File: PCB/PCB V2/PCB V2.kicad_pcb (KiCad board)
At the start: 2 copper layers, 100 x 100 mm, 57 parts, among them J1 Screw_Terminal_01x03, J2 Screw_Terminal_01x03, J3 USB_B, J4 Conn_01x02_Pin, K1 Relay_SPDT, K2 Relay_SPDT, Q1 S8050, Q2 S8050, Q3 S8050, SW1 On/Off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

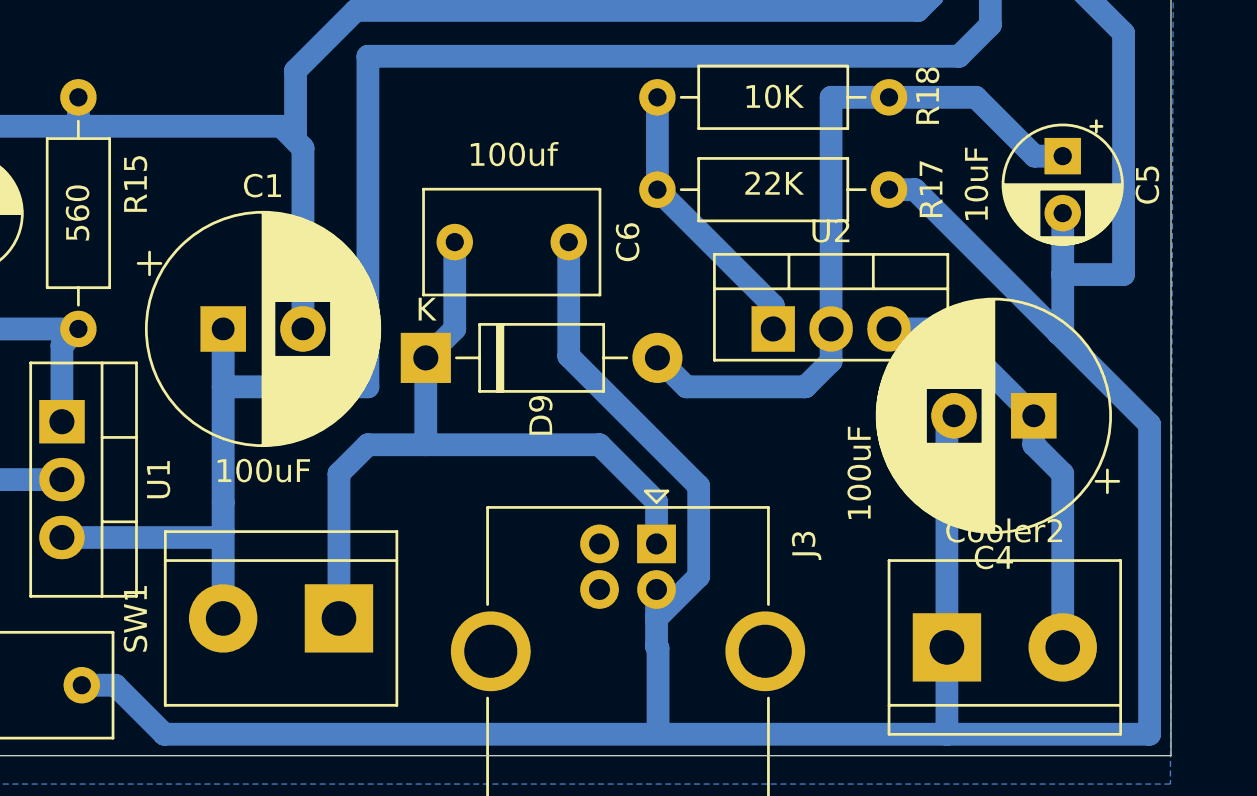
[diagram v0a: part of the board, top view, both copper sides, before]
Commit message: Cambiado el footprint del capacitor
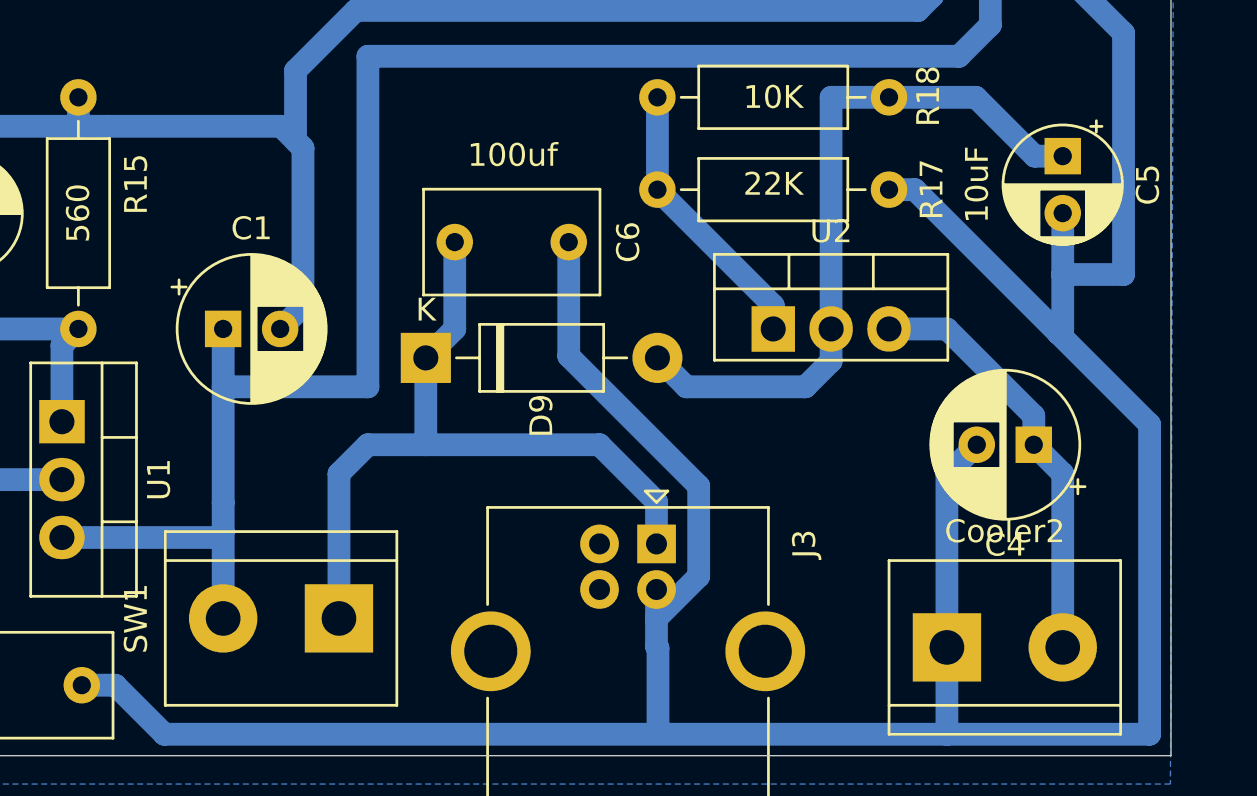
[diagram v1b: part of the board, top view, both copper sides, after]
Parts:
- C1, C4: footprint Capacitor_THT:CP_Radial_D10.0mm_P3.50mm -> Capacitor_THT:CP_Radial_D6.3mm_P2.50mm
- moved C4 1.27 mm to (194.3, 121.9)

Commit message: .
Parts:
- renumbered VCC2 to 3V3, VCC1 to 5V, Cooler2 to BATERIA
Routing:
- net +3.3V: track 339.2 -> 345.3 mm
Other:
- board text added: "GND"
- board text added: "SCL"
- board text added: "SDA"
- board text added: "VCC"
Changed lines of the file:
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@@
 		)
 		(fp_text user "INA219"
-			(at 10.16 0.23 -90)
-			(layer "F.Fab")
+			(at 10.16 0.23 270)
+			(layer "F.SilkS")
 			(effects
 				(font
@@
 		(at 201.295 69.9375 -90)
 		(property "Reference" "ESP-1"
-			(at 0 0.5 90)
+			(at 13.8825 22.225 90)
 			(layer "F.SilkS")
 			(effects
@@
 		(model "C:/Users/47698187/Documents/GitHub/Modelos-3D/Borneras - Conectores/Azules/Doble.step"
 			(offset
-				(xyz -10.25 -4.75 4)
+				(xyz -10.25 -4.75 5)
 			)
 			(scale
@@
 		)
 		(property "Value" "SW_Push"
-			(at -3.175 0 90)
+			(at -3.175 0 180)
 			(layer "F.SilkS")
 			(effects
@@
 		(descr "Through hole straight pin header, 1x01, 2.54mm pitch, single row")
 		(tags "Through hole pin header THT 1x01 2.54mm single row")
-		(property "Reference" "VCC1"
+		(property "Reference" "5V"
 			(at 2.2606 -0.2032 90)
 			(layer "F.SilkS")
@@
 		)
 		(property "Value" "22K"
-			(at 5.08 2.37 180)
-			(layer "F.Fab")
+			(at 5.08 0.179106 180)
+			(layer "F.SilkS")
 			(effects
 				(font
@@
 		(tags "terminal block bornier2")
 		(property "Reference" "SW1"
-			(at 8.89 0 -90)
+			(at 2.54 6.35 -90)
 			(layer "F.SilkS")
 			(effects
@@
 		(model "C:/Users/47698187/Documents/GitHub/Modelos-3D/Borneras - Conectores/Azules/Doble.step"
 			(offset
-				(xyz 15.25 4.75 4.5)
+				(xyz 15.25 4.75 5)
 			)
 			(scale
@@
 		(descr "Through hole straight pin header, 1x01, 2.54mm pitch, single row")
 		(tags "Through hole pin header THT 1x01 2.54mm single row")
-		(property "Reference" "VCC2"
-			(at 0 -2.33 0)
+		(property "Reference" "3V3"
+			(at 3.81 0 90)
 			(layer "F.SilkS")
 			(effects
@@
 		(descr "simple 2-pin terminal block, pitch 5.08mm, revamped version of bornier2")
 		(tags "terminal block bornier2")
-		(property "Reference" "Cooler2"
-			(at 2.54 -5.08 0)
+		(property "Reference" "BATERIA"
+			(at -2.54 -5.08 0)
 			(layer "F.SilkS")
 			(effects
@@
 	)
 	(gr_line
-		(start 165.1 62.23)
-		(end 157.226 62.23)
+		(start 165.1 66.04)
+		(end 157.226 66.04)
 		(stroke
 			(width 1)
@@
 		)
 	)
+	(gr_text "SDA"
+		(at 160.591666 62.248821 0)
+		(layer "F.SilkS")
+		(effects
+			(font
+				(size 1 1)
+				(thickness 0.1)
+			)
+			(justify left bottom)
+		)
+	)
 	(gr_text "GRUPO8 5B"
 		(at 100.33 49.53 0)
@@
 		)
 	)
+	(gr_text "VCC"
+		(at 163.38223 62.214423 0)
+		(layer "F.SilkS")
+		(effects
+			(font
+				(size 1 1)
+				(thickness 0.1)
+			)
+			(justify left bottom)
+		)
+	)
+	(gr_text "GND"
+		(at 166.37 62.23 0)
+		(layer "F.SilkS")
+		(effects
+			(font
+				(size 1 1)
+				(thickness 0.1)
+			)
+			(justify left bottom)
+		)
+	)
+	(gr_text "SCL"
+		(at 157.48 62.23 0)
+		(layer "F.SilkS")
+		(effects
+			(font
+				(size 1 1)
+				(thickness 0.1)
+			)
+			(justify left bottom)
+		)
+	)
 	(via
 		(at 105.3084 40.7416)
@@
 	)
 	(segment
-		(start 157.285 62.23)
-		(end 165.1 62.23)
+		(start 161.095 66.037207)
+		(end 165.102793 66.037207)
+		(width 1)
+		(layer "F.Cu")
+		(net 3)
+	)
+	(segment
+		(start 161.095 66.04)
+		(end 161.095 66.037207)
+		(width 1)
+		(layer "F.Cu")
+		(net 3)
+	)
+	(segment
+		(start 157.285 66.04)
+		(end 161.095 66.04)
 		(width 1)
 		(layer "F.Cu")
@@
 	)
 	(via
-		(at 165.1 62.23)
+		(at 165.102793 66.037207)
 		(size 1.6)
 		(drill 0.8)
@@
 	)
 	(via
-		(at 157.285 62.23)
+		(at 157.285 66.04)
 		(size 1.6)
 		(drill 0.8)
@@
 	)
 	(segment
+		(start 157.285 66.04)
+		(end 157.285 42.985)
+		(width 1)
+		(layer "B.Cu")
+		(net 3)
+	)
+	(segment
 		(start 182.86 53.34)
 		(end 182.86 65.757167)
@@
 	)
 	(segment
+		(start 132.480151 39.81)
+		(end 129.38 42.910151)
+		(width 1)
+		(layer "B.Cu")
+		(net 3)
+	)
+	(segment
 		(start 125.6 113.03)
 		(end 127.7 110.93)
@@
 	)
 	(segment
+		(start 165.102793 66.037207)
+		(end 165.102793 64.767207)
+		(width 1)
+		(layer "B.Cu")
+		(net 3)
+	)
+	(segment
 		(start 104.0638 52.6034)
 		(end 101.07 55.5972)
@@
 	)
 	(segment
+		(start 154.11 39.81)
+		(end 132.480151 39.81)
+		(width 1)
+		(layer "B.Cu")
+		(net 3)
+	)
+	(segment
 		(start 183.142833 66.04)
 		(end 182.86 65.757167)
@@
 	)
 	(segment
+		(start 157.285 42.985)
+		(end 154.11 39.81)
+		(width 1)
+		(layer "B.Cu")
+		(net 3)
+	)
+	(segment
 		(start 147.36 132.280136)
 		(end 147.36 127.04)
@@
 	)
 	(segment
-		(start 167.64 62.23)
-		(end 167.9725 61.8975)
+		(start 129.38 56.515)
+		(end 116.84 56.515)
 		(width 1)
 		(layer "B.Cu")
@@
 	)
 	(segment
-		(start 116.84 56.515)
-		(end 129.38 56.515)
+		(start 144.78 113.03)
+		(end 144.78 115.57)
 		(width 1)
 		(layer "B.Cu")
@@
 	)
 	(segment
-		(start 144.78 113.03)
-		(end 144.78 115.57)
+		(start 101.07 98.959849)
+		(end 105.265151 103.155)
 		(width 1)
 		(layer "B.Cu")
@@
 	)
 	(segment
-		(start 101.07 98.959849)
-		(end 105.265151 103.155)
+		(start 165.102793 64.767207)
+		(end 167.9725 61.8975)
 		(width 1)
 		(layer "B.Cu")
@@
 	)
 	(segment
+		(start 129.38 42.910151)
+		(end 129.38 56.515)
+		(width 1)
+		(layer "B.Cu")
+		(net 3)
+	)
+	(segment
 		(start 112.9284 52.6034)
 		(end 104.0638 52.6034)
@@
 	)
 	(segment
-		(start 129.38 56.515)
-		(end 129.38 42.910151)
-		(width 1)
-		(layer "B.Cu")
-		(net 3)
-	)
-	(segment
-		(start 129.38 42.910151)
-		(end 132.480151 39.81)
-		(width 1)
-		(layer "B.Cu")
-		(net 3)
-	)
-	(segment
 		(start 147.32 127)
 		(end 147.32 123.19)
@@
 	)
 	(segment
-		(start 165.1 62.23)
-		(end 167.64 62.23)
-		(width 1)
-		(layer "B.Cu")
-		(net 3)
-	)
-	(segment
 		(start 128.27 104.08)
 		(end 128.27 110.36)
@@
 	)
 	(segment
-		(start 157.285 42.985)
-		(end 157.285 62.23)
-		(width 1)
-		(layer "B.Cu")
-		(net 3)
-	)
-	(segment
 		(start 144.78 120.65)
 		(end 147.32 123.19)
@@
 	)
 	(segment
-		(start 132.480151 39.81)
-		(end 154.11 39.81)
-		(width 1)
-		(layer "B.Cu")
-		(net 3)
-	)
-	(segment
 		(start 109.92 102.760534)
 		(end 109.525534 103.155)
@@
 	)
 	(segment
-		(start 154.11 39.81)
-		(end 157.285 42.985)
-		(width 1)
-		(layer "B.Cu")
-		(net 3)
-	)
-	(segment
 		(start 116.84 56.515)
 		(end 112.9284 52.6034)
@@
 		(hatch edge 0.5)
 		(connect_pads
-			(clearance 1)
+			(clearance 1.5)
 		)
 		(min_thickness 0.25)

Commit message: .
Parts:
- removed R15: 560, Resistor_THT:R_Axial_DIN0207_L6.3mm_D2.5mm_P10.16mm_Horizontal
- removed R16: 330, Resistor_THT:R_Axial_DIN0207_L6.3mm_D2.5mm_P10.16mm_Horizontal
- added RV1: R_Potentiometer, Potentiometer_THT:Potentiometer_Bourns_3386W_Horizontal, F.Cu at (152.4, 108.0)
- moved C2 2.54 mm to (144.8, 113.0)
- renumbered BATERIA to Cooler2, 5V to VCC1, 3V3 to VCC2
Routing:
- net GND: track 556.2 -> 537.1 mm
- net +3.3V: track 345.3 -> 352.2 mm
- net Net-(U1-ADJ): track 9.45 -> 16.1 mm
